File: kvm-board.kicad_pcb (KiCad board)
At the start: 2 copper layers, 65.4 x 31.4 mm, 21 parts, among them J1 TYPE-C-31-M-12, J2 TYPE-C-31-M-12, U1 CH9329, U2 CH340N

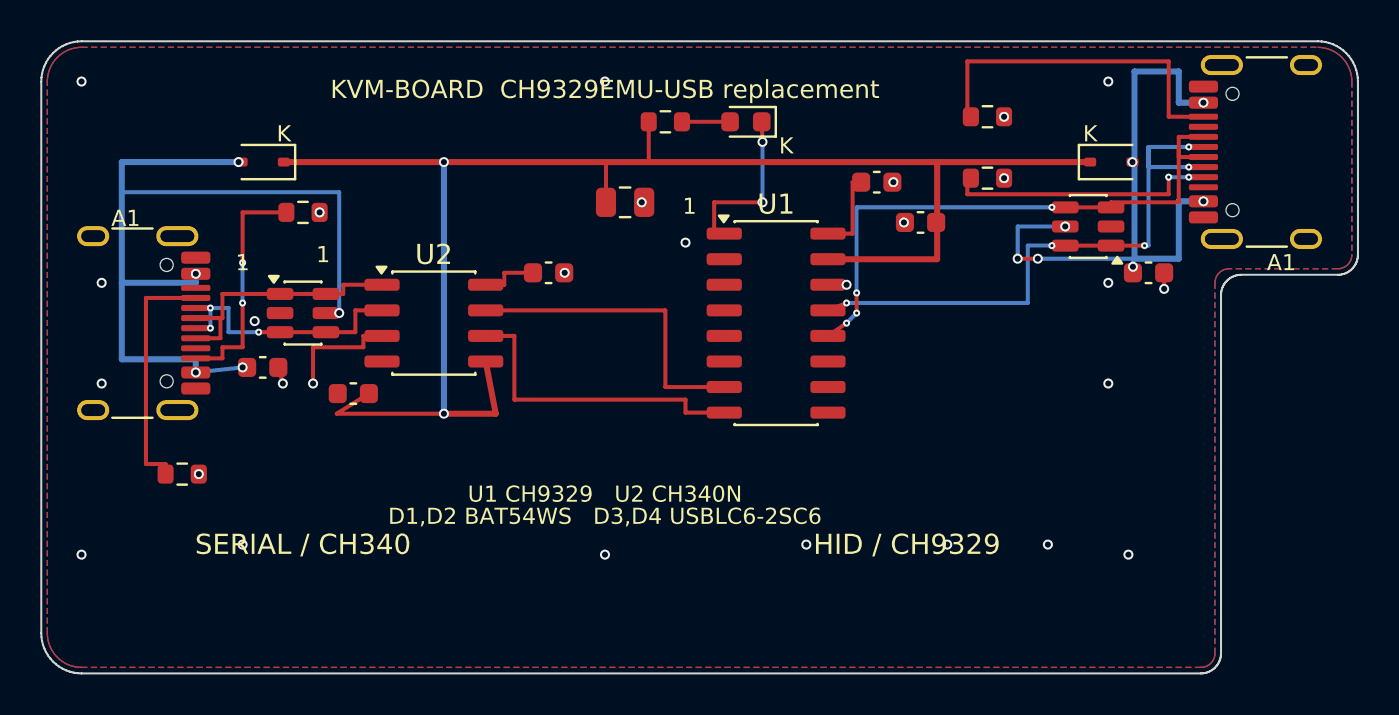
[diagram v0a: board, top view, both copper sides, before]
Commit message: Move J1/J2 out so plugs clear the case wall
J1 now overhangs the left edge by 1.5 mm and J2 the right edge by 1.4 mm. J2 stops at 1.4 mm because its front shell pad would otherwise clash with the top-right R2 corner; it also moves down 0.2 mm. Adjust the J1 VBUS/CC1 escapes for the new pad positions and regenerate the board, fabrication outputs, images and 1:1 print sheet. DRC and ERC are clean.
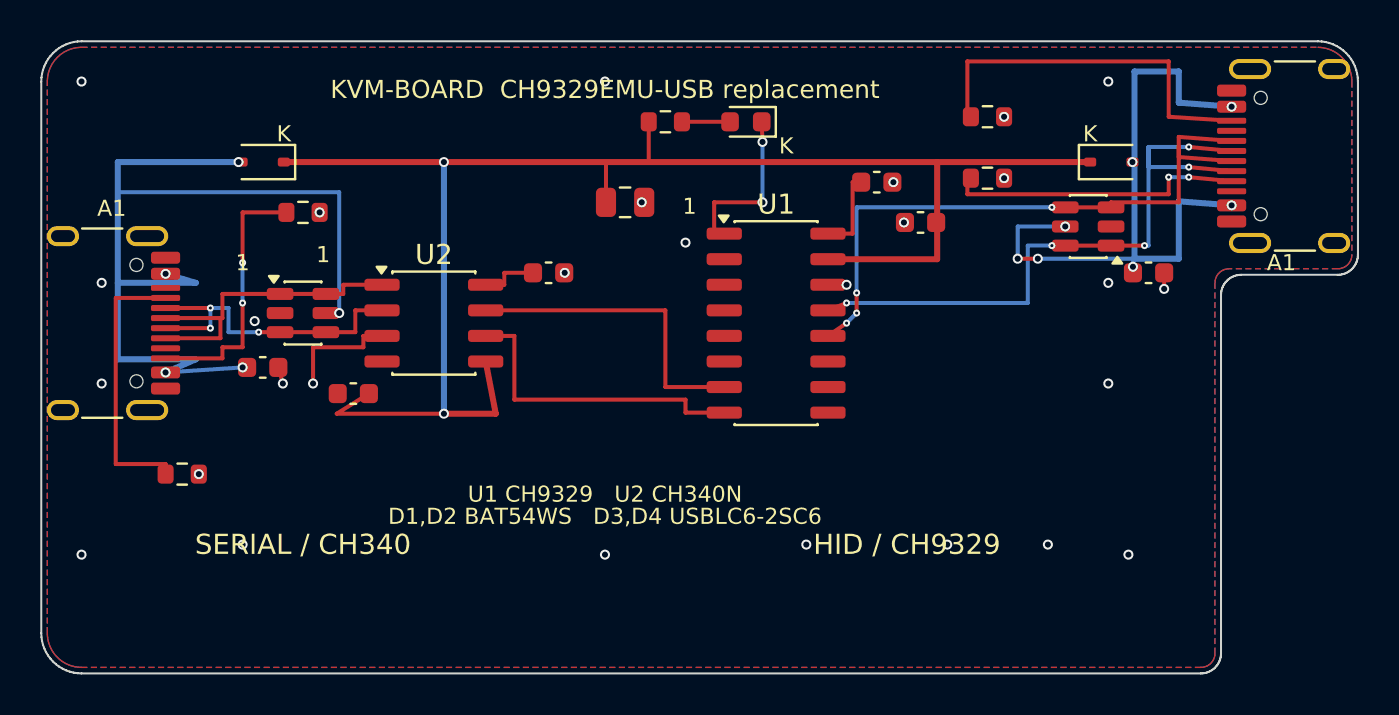
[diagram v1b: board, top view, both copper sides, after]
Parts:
- moved J1 1.50 mm to (2.13, 14.0)
- moved J2 1.41 mm to (63.2, 5.70)
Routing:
- net VBUS_SER: track 44.2 -> 48.6 mm
- net USB_SER_DP: track 13.1 -> 16.1 mm
- net USB_SER_DM: track 13.3 -> 16.3 mm
- net USB_HID_DM: track 30.2 -> 33.0 mm
- net VBUS_HID: track 31.1 -> 33.9 mm
- net USB_HID_DP: track 29.5 -> 32.3 mm
- net CC2_SER: track 11.8 -> 13.3 mm
- net CC1_SER: track 12.2 -> 13.7 mm
- net CC1_HID: track 13.6 -> 15.0 mm
- net CC2_HID: track 17.4 -> 18.8 mm

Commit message: Add SET/GND test pads and a repository QR code
TP1/TP2 break out the CH9329 SET pin and GND so the WCH config tool can be used without soldering to U1. Both are bare 1.7 mm pads on 2.54 mm pitch and are excluded from the BOM and CPL.

The bottom silkscreen now carries a QR code for https://github.com/nananek/kvm-board. The matrix is checked in as scripts/repo_qr.txt; scripts/make_repo_qr.py regenerates it when the URL changes.
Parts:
- added TP1: SET, TestPoint_1P, F.Cu at (42.0, 17.0)
- added TP2: GND, TestPoint_1P, F.Cu at (44.5, 17.0)
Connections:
- U1 pad 11: (no net) -> SET
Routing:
- net SET: track 0.00 -> 3.21 mm
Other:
- board text added: "GND"
- board text added: "SET"
- board text added: "SHORT TO CONFIGURE"

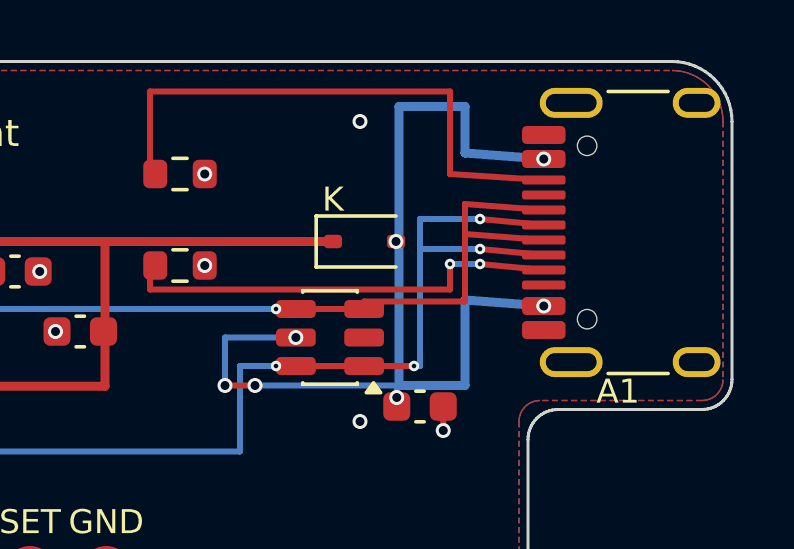
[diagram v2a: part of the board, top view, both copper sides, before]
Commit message: Tidy HID USB D- routing
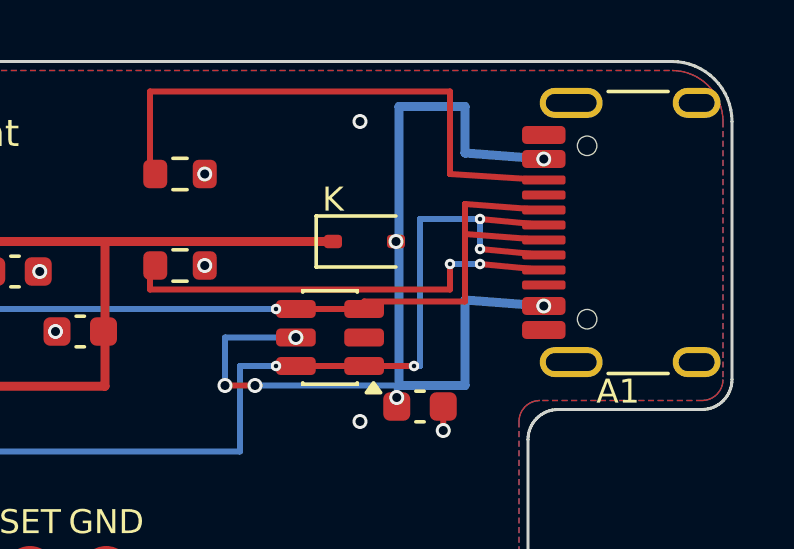
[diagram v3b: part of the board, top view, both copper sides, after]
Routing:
- net USB_HID_DM: track 33.0 -> 31.0 mm
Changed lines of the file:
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@@
-	)
-	(segment
-		(start 55 6.25)
-		(end 57 6.25)
-		(width 0.2)
-		(layer "B.Cu")
-		(net "USB_HID_DM")
 	)
 	(segment
@@
 	)
 	(segment
-		(start 55 5.25)
-		(end 55 6.25)
+		(start 57 5.25)
+		(end 57 6.25)
 		(width 0.2)
 		(layer "B.Cu")
